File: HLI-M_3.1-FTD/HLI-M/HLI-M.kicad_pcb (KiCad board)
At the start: 2 copper layers, 124.2 x 84.7 mm, 119 parts, among them CON1 , CON2 USB_B, CON3 , CON4 Connector_Adapter, CON5 Connector_Audio, CON6 Conn_01x15, CON7 Conn_01x09, CON8 CR123A, Q1 IRLML5103, Q2 BC817, Q3 BC817, Q4 BSS84, Q5 BSS84, Q6 BSS84, Q7 BSS84, U1 PIC24HJ64GP206-I_PT, U10 24AA02-OT, U10-A SOIC-8_3.9x4.9mm_P1.27mm, U11 ULN2003, U12 ULN2003, U13 ULN2003, U2 SOIC-8_3.9x4.9mm_P1.27mm, U2-A DFN-8-1EP_6x5mm_P1.27mm_EP2x2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, U3 MAX3232, U4 TPS7A0533PDBV, U5 TPS7A0533PDBV, U6 VSON-10-1EP_3x3mm_P0.5mm_EP1.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, U8 FT232RL, U9 SOIC-8_3.9x4.9mm_P1.27mm, Y1 Crystal_32KHz, Y2 Crystal_20MHz

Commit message: att
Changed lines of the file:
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@@
     (fp_line (start -9.99 6.67) (end -9.99 -3.83) (layer "F.SilkS") (width 0.12))
     (fp_line (start -8.93 -4.89) (end 42.17 -4.89) (layer "F.SilkS") (width 0.12))
-    (fp_arc (start 33.851689 -2.79) (mid 35.123329 -2.197033) (end 35.48647 -0.841744) (layer "F.SilkS") (width 0.12))
+    (fp_arc (start 33.851689 -2.79) (mid 35.123331 -2.197031) (end 35.48647 -0.841744) (layer "F.SilkS") (width 0.12))
     (fp_arc (start 42.17 -4.89) (mid 42.919533 -4.579533) (end 43.23 -3.83) (layer "F.SilkS") (width 0.12))
     (fp_arc (start 43.23 6.67) (mid 42.919533 7.419533) (end 42.17 7.73) (layer "F.SilkS") (width 0.12))
-    (fp_arc (start 34.587202 4.258256) (mid 34.019453 5.24164) (end 32.952421 5.63) (layer "F.SilkS") (width 0.12))
+    (fp_arc (start 34.587202 4.258256) (mid 34.01945 5.241642) (end 32.952421 5.63) (layer "F.SilkS") (width 0.12))
     (fp_arc (start -8.93 7.73) (mid -9.679533 7.419533) (end -9.99 6.67) (layer "F.SilkS") (width 0.12))
     (fp_arc (start -2.24647 -0.841744) (mid -1.883323 -2.197028) (end -0.611689 -2.79) (layer "F.SilkS") (width 0.12))
@@
     (fp_arc (start 0.276073 5.57) (mid -0.752387 5.195671) (end -1.299619 4.247837) (layer "F.Fab") (width 0.1))
     (fp_arc (start 42.17 -4.83) (mid 42.877107 -4.537107) (end 43.17 -3.83) (layer "F.Fab") (width 0.1))
-    (fp_arc (start 33.863194 -2.73) (mid 35.088869 -2.158463) (end 35.438886 -0.852163) (layer "F.Fab") (width 0.1))
+    (fp_arc (start 33.863194 -2.73) (mid 35.08887 -2.158462) (end 35.438886 -0.852163) (layer "F.Fab") (width 0.1))
     (fp_arc (start -2.198886 -0.852163) (mid -1.848865 -2.15846) (end -0.623194 -2.73) (layer "F.Fab") (width 0.1))
     (fp_arc (start 43.17 6.67) (mid 42.877107 7.377107) (end 42.17 7.67) (layer "F.Fab") (width 0.1))
-    (fp_arc (start 34.539619 4.247837) (mid 33.99238 5.195662) (end 32.963927 5.57) (layer "F.Fab") (width 0.1))
+    (fp_arc (start 34.539619 4.247837) (mid 33.992389 5.195681) (end 32.963927 5.57) (layer "F.Fab") (width 0.1))
     (fp_arc (start -8.93 7.67) (mid -9.637107 7.377107) (end -9.93 6.67) (layer "F.Fab") (width 0.1))
     (fp_arc (start -9.93 -3.83) (mid -9.637107 -4.537107) (end -8.93 -4.83) (layer "F.Fab") (width 0.1))
@@
   (segment (start 187.6552 92.0242) (end 185.4746 89.8436) (width 1.5) (layer "B.Cu") (net 26))
   (segment (start 113.9571 109.1311) (end 116.1542 111.3282) (width 1.5) (layer "B.Cu") (net 26))
-  (segment (start 102.2604 110.998) (end 112.0902 110.998) (width 1.5) (layer "B.Cu") (net 26))
-  (segment (start 74.295 53.1368) (end 74.295 78.4352) (width 1.5) (layer "B.Cu") (net 26))
+  (segment (start 102.9716 110.998) (end 112.0902 110.998) (width 1.5) (layer "B.Cu") (net 26))
   (segment (start 162.4584 109.5248) (end 164.3634 111.4298) (width 1.5) (layer "B.Cu") (net 26))
-  (segment (start 112.0902 110.998) (end 113.9571 109.1311) (width 1.5) (layer "B.Cu") (net 26))
   (segment (start 164.3634 111.4298) (end 164.3634 111.4806) (width 1.5) (layer "B.Cu") (net 26))
   (segment (start 164.3634 111.4806) (end 173.7868 111.4806) (width 1.5) (layer "B.Cu") (net 26))
+  (segment (start 112.0902 110.998) (end 113.9571 109.1311) (width 1.5) (layer "B.Cu") (net 26))
   (segment (start 184.0992 67.4116) (end 181.7037 67.4116) (width 1.5) (layer "B.Cu") (net 26))
   (segment (start 185.4746 89.8436) (end 184.5564 89.8436) (width 1.5) (layer "B.Cu") (net 26))
   (segment (start 187.1218 70.4342) (end 184.0992 67.4116) (width 1.5) (layer "B.Cu") (net 26))
-  (segment (start 89.6874 93.8276) (end 89.6874 98.425) (width 1.5) (layer "B.Cu") (net 26))
   (segment (start 184.5564 89.8436) (end 184.7812 89.8436) (width 1.5) (layer "B.Cu") (net 26))
-  (segment (start 89.6874 98.425) (end 102.2604 110.998) (width 1.5) (layer "B.Cu") (net 26))
+  (segment (start 74.295 82.3214) (end 102.9716 110.998) (width 1.5) (layer "B.Cu") (net 26))
   (segment (start 92.4589 38.862) (end 79.0448 38.862) (width 1.5) (layer "B.Cu") (net 26))
   (segment (start 96.5454 34.7755) (end 92.4589 38.862) (width 1.5) (layer "B.Cu") (net 26))
   (segment (start 74.295 43.6118) (end 74.295 53.1368) (width 1.5) (layer "B.Cu") (net 26))
-  (segment (start 74.295 78.4352) (end 89.6874 93.8276) (width 1.5) (layer "B.Cu") (net 26))
   (segment (start 187.1218 87.503) (end 187.1218 70.4342) (width 1.5) (layer "B.Cu") (net 26))
+  (segment (start 74.295 53.1368) (end 74.295 82.3214) (width 1.5) (layer "B.Cu") (net 26))
   (segment (start 160.655 111.3282) (end 162.4584 109.5248) (width 1.5) (layer "B.Cu") (net 26))
   (segment (start 187.6552 97.6122) (end 187.6552 92.0242) (width 1.5) (layer "B.Cu") (net 26))

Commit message: atualizado hli-m, precisa de revisao
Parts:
- added RT3: 0.5A, Resistor_SMD:R_1812_4532Metric, F.Cu at (74.3, 44.5)
- L1: renamed from L2; value BLM21PG221SN1D -> BBPY0020
- Q1: value IRLML5103 -> DMP3068L-7
- R4: value 10k -> 22k
- moved RT1 8.34 mm to (98.3, 44.4)
- moved LED1 7.00 mm to (88.6, 45.5), turned to 180 degrees
- moved R5 4.03 mm to (167.6, 70.7), turned to 0 degrees
- moved C14 3.97 mm to (167.6, 66.6), turned to 180 degrees
- moved C1 2.99 mm to (98.0, 52.4)
- moved C2 2.99 mm to (100.2, 52.4)
- moved C3 2.99 mm to (102.3, 52.3)
- moved R1 2.84 mm to (84.8, 45.5)
- moved R21 2.60 mm to (133.3, 91.6)
- moved C4 1.17 mm to (117.2, 50.4)
- moved L1 1.17 mm to (119.2, 50.5)
- moved R22 1.09 mm to (131.5, 91.6)
- moved Q5 0.86 mm to (132.6, 95.8), turned to -90 degrees
- moved C13 0.33 mm to (167.6, 68.6), turned to 0 degrees
- moved CON1 0.30 mm to (88.6, 34.8)
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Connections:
- C21 pad 1: Net-(U1-Pad40) -> Net-(C21-Pad1)
- C22 pad 1: Net-(U1-Pad39) -> Net-(C22-Pad1)
- CON1 pad 1: +5V -> Net-(CON1-Pad1)
- CON3 pad 23: K_E -> 0
- CON8 pad N: (no net) -> 0
- U1 pad 4: Net-(C18-Pad1) -> Net-(C14-Pad1)
- U1 pad 56: Net-(C24-Pad1) (its old number) -> Net-(C19-Pad1)
- U2 pad 3: Net-(R16-Pad2) -> Net-(R5-Pad2)
- U2 pad 6: Net-(C18-Pad1) -> Net-(C14-Pad1)
- U2 pad 7: Net-(R16-Pad2) -> Net-(R5-Pad2)
- U2-A pad 3: Net-(R16-Pad2) -> Net-(R5-Pad2)
- U2-A pad 6: Net-(C18-Pad1) -> Net-(C14-Pad1)
- U2-A pad 7: Net-(R16-Pad2) -> Net-(R5-Pad2)
- U6 pad 8: Net-(R4-Pad2) -> Net-(R2-Pad2)
- U6 pad 9: Net-(R5-Pad1) -> Net-(R3-Pad1)
- Y2 pad 1: Net-(U1-Pad39) -> Net-(C22-Pad1)
- Y2 pad 3: Net-(U1-Pad40) -> Net-(C21-Pad1)
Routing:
- net +12V: track 261.5 -> 352.8 mm, vias 1 -> 5
- net Net-(C14-Pad1): track 0.00 -> 30.3 mm, vias 0 -> 2
- net Net-(R5-Pad2): track 0.00 -> 26.6 mm, vias 0 -> 2
- net Net-(C18-Pad1): track 23.5 -> 0.00 mm, vias 2 -> 0
- net K_E: track 24.6 -> 1.38 mm
- net Net-(R16-Pad2): track 16.8 -> 0.00 mm
- net +5V: track 243.3 -> 259.2 mm, vias 0 -> 2
- net Net-(CON1-Pad1): track 0.00 -> 12.5 mm
- net Net-(U1-Pad39): track 10.4 -> 0.00 mm
- net Net-(C22-Pad1): track 0.00 -> 10.4 mm
- net Net-(CON3-Pad24): track 52.5 -> 44.2 mm
- net Net-(U1-Pad40): track 7.80 -> 0.00 mm
- net Net-(C21-Pad1): track 0.00 -> 7.80 mm
- net +3V3: track 293.1 -> 286.7 mm, vias 28 -> 29
- net Net-(R2-Pad2): track 0.00 -> 4.99 mm
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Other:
- board size 124.2 x 84.7 mm -> 125.2 x 85.6 mm

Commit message: att
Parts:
- removed G***: LOGO, LOGO
- removed RT3: 0.5A, Resistor_SMD:R_1812_4532Metric
- added F1: Fuse, Fuse:Fuse_1812_4532Metric, F.Cu at (71.3, 44.9)
- added RV1: Varistor, Capacitor_SMD:C_0603_1608Metric_Pad1.08x0.95mm_HandSolder, F.Cu at (76.0, 45.9)
- CON5: value Connector_Audio -> Connector_note; footprint Connector_JST:JST_EH_B3B-EH-A_1x03_P2.50mm_Vertical -> Connector_IDC:IDC-Header_2x04_P2.54mm_Horizontal
- moved G1 104.6 mm to (93.3, 108.3)
- moved CON5 18.9 mm to (180.4, 76.5), turned to 0 degrees
- moved CON4 14.3 mm to (180.6, 48.1)
- moved LED1 2.06 mm to (90.6, 44.9)
- moved R1 2.06 mm to (86.8, 44.9)
- moved R8 1.62 mm to (175.6, 87.8)
- moved R9 1.62 mm to (177.4, 87.8)
- moved CON8 0.97 mm to (83.5, 80.7)
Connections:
- CON5 pad 2: 0 -> INIB
- CON5 pad 3: +12V -> RXA
- CON8 pad P: (no net) -> Net-(CON8-Pad1)
- U1 pad 17: Net-(R9-Pad1) -> Net-(R7-Pad1)
- U1 pad 44: (no net) -> EXTERN_D10
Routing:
- net PRINT_IMP: track 15.7 -> 114.0 mm
- net INIB: track 27.3 -> 124.6 mm, vias 1 -> 2
- net NOTE_: track 14.8 -> 80.8 mm, vias 0 -> 2
- net RXA: track 43.5 -> 106.0 mm, vias 2 -> 3
- net EXTERN_D10: track 0.00 -> 59.4 mm, vias 0 -> 2
- net TXA: track 46.0 -> 96.1 mm, vias 2 -> 5
- net Net-(R7-Pad1): track 0.00 -> 35.2 mm, vias 0 -> 2
- net Net-(R9-Pad1): track 33.7 -> 0.00 mm, vias 2 -> 0
- net +5V: track 259.2 -> 235.9 mm
- net PGED2: track 45.0 -> 66.7 mm
- net PGEC2: track 43.7 -> 64.7 mm
- net VBAT: track 208.2 -> 223.8 mm
- net RESET: track 33.8 -> 44.7 mm
- net +3V3: track 286.7 -> 295.7 mm
- net TXP: track 85.1 -> 76.3 mm
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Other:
- board size 125.2 x 85.6 mm -> 125.2 x 86.4 mm

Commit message: att projeto
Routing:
- net +12V: track 360.9 -> 393.0 mm, vias 5 -> 6
- net EXTERN_D10: track 59.4 -> 57.5 mm
- net 0: vias 45 -> 46

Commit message: atualização circuito FTD e 3D
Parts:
- added R29: 470R, Resistor_SMD:R_0603_1608Metric_Pad0.98x0.95mm_HandSolder, F.Cu at (107.3, 58.8)
- added R30: 470R, Resistor_SMD:R_0603_1608Metric_Pad0.98x0.95mm_HandSolder, F.Cu at (104.8, 58.8)
- C21, C22: value 10pF -> 20pF
- C23, C24: value 7pF -> 12pF
- moved RV1 6.94 mm to (71.3, 51.0), turned to 0 degrees
- moved LED1 1.82 mm to (90.8, 46.7)
- moved R1 1.82 mm to (87.0, 46.7)
- moved F1 1.55 mm to (71.5, 46.4)
- moved C10 1.27 mm to (100.7, 68.8)
- moved R17 1.18 mm to (140.0, 57.4)
- moved C2 1.09 mm to (99.1, 52.3)
- moved U8 1.09 mm to (109.0, 51.3)
- moved C3 1.09 mm to (101.2, 52.3)
- moved C1 1.09 mm to (96.9, 52.3)
- moved Q3 0.94 mm to (140.1, 60.5)
- moved R18 0.73 mm to (140.2, 63.7)
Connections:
- C14 pad 1: Net-(C14-Pad1) -> Net-(U1-SCK2/RG6)
- C19 pad 1: Net-(C19-Pad1) -> Net-(U1-VDDCORE)
- C20 pad 1: Net-(C19-Pad1) -> Net-(U1-VDDCORE)
- C23 pad 1: Net-(C23-Pad1) -> Net-(U1-RC14)
- C24 pad 1: Net-(C24-Pad1) -> Net-(U1-RC13)
- C8 pad 1: Net-(C8-Pad1) -> Net-(U6-USB_SEL)
- CON8 pad P: Net-(CON8-Pad1) -> (no net)
- R12 pad 2: Net-(C19-Pad1) -> Net-(U1-VDDCORE)
- R2 pad 2: Net-(R2-Pad2) -> Net-(U6-ISET)
- R3 pad 1: Net-(R3-Pad1) -> Net-(U6-TS)
- R5 pad 2: Net-(R5-Pad2) -> Net-(U2-*HOLD)
- R6 pad 1: Net-(R6-Pad1) -> Net-(U1-RD8)
- R7 pad 1: Net-(R7-Pad1) -> Net-(U1-RB6)
- RT2 pad 1: Net-(CON8-Pad1) -> Net-(CON8-+)
- U3 pad 11: Net-(U1-Pad33) -> Net-(U1-U1TX/RF3)
- U3 pad 12: Net-(U1-Pad34) -> Net-(U1-U1RX/RF2)
- U8 pad 1: TXA -> Net-(U8-TXD)
- U8 pad 5: RXA -> Net-(U8-RXD)
- Y1 pad 1: Net-(C23-Pad1) -> Net-(U1-RC14)
- Y1 pad 2: Net-(C24-Pad1) -> Net-(U1-RC13)
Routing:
- net Net-(CON8-Pad1): track 19.2 -> 0.00 mm
- net Net-(CON8-+): track 0.00 -> 19.2 mm
- net Net-(U1-Pad39): track 0.00 -> 10.4 mm
- net Net-(U1-OSC1/CLKIN): track 10.4 -> 0.00 mm
- net Net-(U1-Pad40): track 0.00 -> 7.80 mm
- net Net-(U1-OSC2/CLKO): track 7.80 -> 0.00 mm
- net +5V: track 235.9 -> 240.5 mm
- net +5VL: track 56.6 -> 60.4 mm
- net Net-(U8-TXD): track 0.00 -> 3.34 mm
- net Net-(U8-RXD): track 0.00 -> 3.03 mm
- net Net-(CON1-Pin_1): track 15.2 -> 18.0 mm
- net RXA: track 106.0 -> 104.1 mm
- net +3V3: track 295.7 -> 294.0 mm
- net TXA: track 96.1 -> 94.7 mm
- net INIB: track 124.6 -> 123.4 mm
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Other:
- board size 125.2 x 86.4 mm -> 125.2 x 86.1 mm
- board text added: "Made in China"
- board text removed: "Designed in Brazil. Made in China"

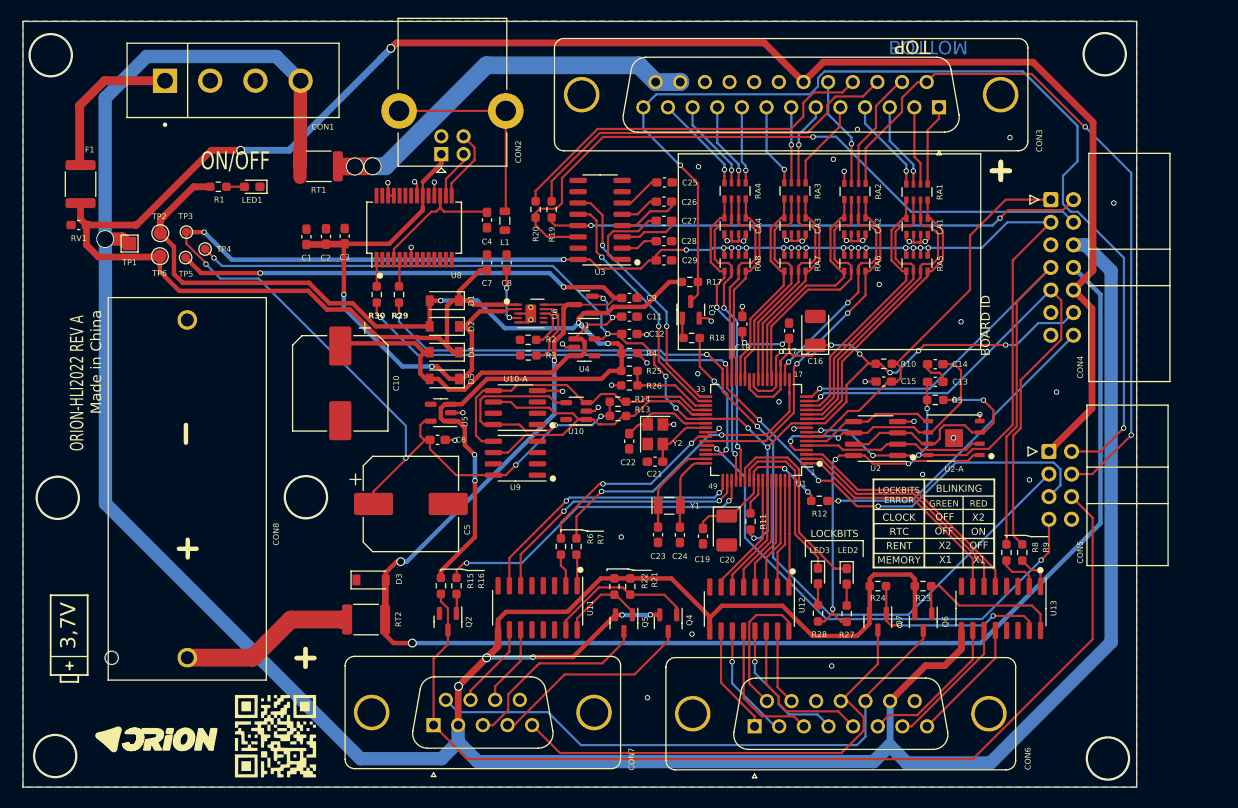
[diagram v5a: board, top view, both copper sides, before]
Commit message: HLI-M_2023: circuito atualizado e revisado.
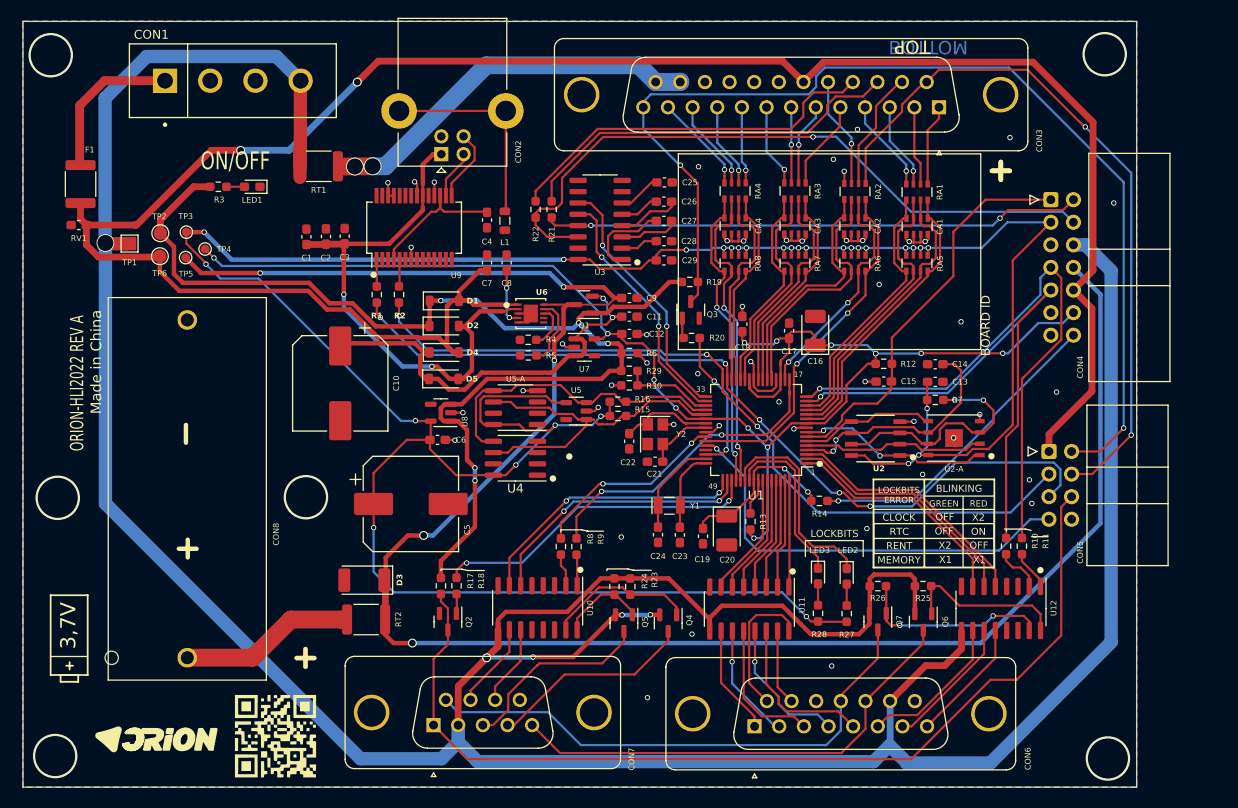
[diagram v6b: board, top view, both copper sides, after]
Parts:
- CON1: footprint 6:Molex-0015244449-0 -> Footprint_HLI-M:Molex-0015244449-0
- CON4: value Connector_Adapter -> Con_ADAPTER
- CON5: value Connector_note -> Con_MULTLINKER
- D3: footprint Diode_SMD:D_SOD-123 -> Diode_SMD:D_2010_5025Metric
- Q4, Q5, Q6, Q7: value BSS84 -> DMP2305
- R4: renamed from R2; value 10k -> 3,3K
- U1: value PIC24HJ64GP206-I_PT -> PIC24HJ64GP206
- U2: value SOIC-8_3.9x4.9mm_P1.27mm -> FM25V10; footprint Package_SO:SOIC-8_3.9x4.9mm_P1.27mm -> Footprint_HLI-M:FM25V10-GTR
- U4: renamed from U9; value SOIC-8_3.9x4.9mm_P1.27mm -> ATSHA204A-SSHDA-B
- U6: value VSON-10-1EP_3x3mm_P0.5mm_EP1.2x2mm_ThermalVias -> LM3658SD; footprint Package_SON:VSON-10-1EP_3x3mm_P0.5mm_EP1.2x2mm_ThermalVias -> Footprint_HLI-M:LM3658SD
- moved D3 0.76 mm to (103.4, 90.9), turned to 180 degrees
- moved R10 0.71 mm to (175.6, 87.1)
- moved R11 0.71 mm to (177.3, 87.1)
- moved D5 0.08 mm to (112.3, 68.3), turned to 0 degrees
- moved D2 0.06 mm to (112.4, 62.4), turned to 0 degrees
- turned D4 to 0 degrees
- turned D1 to 0 degrees
- renumbered C24 to C23, C23 to C24, R30 to R1, R8 to R10, R9 to R11, R10 to R12, R11 to R13, R12 to R14, R13 to R15, R14 to R16, R15 to R17, R16 to R18, R17 to R19, R29 to R2, R18 to R20, R19 to R21, R20 to R22, R21 to R23, R22 to R24, R23 to R25, R24 to R26, R25 to R29, R1 to R3, R26 to R30, R3 to R5, R4 to R6, R5 to R7, R6 to R8, R7 to R9, U11 to U10, U12 to U11, U13 to U12, U10 to U5, U10-A to U5-A, U4 to U7, U5 to U8, U8 to U9
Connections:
- C10 pad 1: Net-(D4-A) -> Net-(D4-K)
- C11 pad 1: Net-(D4-A) -> Net-(D4-K)
- C23 pad 1: Net-(U1-RC13) -> Net-(U1-RC14)
- C24 pad 1: Net-(U1-RC14) -> Net-(U1-RC13)
- CON6 pad 12: COUT -> CIN
- CON6 pad 13: CIN -> COUT
- CON8 pad P: (no net) -> Net-(CON8-+)
- D1 pad 1: +5V -> +5VD
- D1 pad 2: +5VD -> +5V
- D2 pad 1: +5VL -> +5VD
- D2 pad 2: +5VD -> +5VL
- D3 pad 1: 0 -> VBAT
- D3 pad 2: VBAT -> 0
- D4 pad 1: +5V -> Net-(D4-K)
- D4 pad 2: Net-(D4-A) -> +5V
- D5 pad 1: +5VL -> Net-(D4-K)
- D5 pad 2: Net-(D4-A) -> +5VL
- Q1 pad 2: Net-(D4-A) -> Net-(D4-K)
- Q6 pad 3: CIN -> COUT
- Q7 pad 3: COUT -> CIN
- R10 pad 1: PGED2 -> PGEC2
- R10 pad 2: PIN-CIN -> PIN-COUT
- R11 pad 1: PGEC2 -> PGED2
- R11 pad 2: PIN-COUT -> PIN-CIN
- R13 pad 2: Net-(R11-Pad2) -> Net-(R13-Pad2)
- U1 pad 17: Net-(R7-Pad1) -> Net-(U1-RB6)
- U1 pad 33: Net-(U1-Pad33) -> Net-(U1-U1TX/RF3)
- U1 pad 34: Net-(U1-Pad34) -> Net-(U1-U1RX/RF2)
- U1 pad 39: Net-(U1-Pad39) -> Net-(U1-OSC1/CLKIN)
- U1 pad 4: Net-(C14-Pad1) -> Net-(U1-SCK2/RG6)
- U1 pad 40: Net-(U1-Pad40) -> Net-(U1-OSC2/CLKO)
- U1 pad 42: Net-(R6-Pad1) -> Net-(U1-RD8)
- U1 pad 47: Net-(C23-Pad1) -> Net-(U1-RC13)
- U1 pad 48: Net-(C24-Pad1) -> Net-(U1-RC14)
- U1 pad 56: Net-(C19-Pad1) -> Net-(U1-VDDCORE)
- U1 pad 57: Net-(R15-Pad2) -> Net-(R13-Pad2)
- U12 pad 1: PIN-COUT -> PIN-CIN
- U12 pad 2: PIN-CIN -> PIN-COUT
- U2 pad 3: Net-(R5-Pad2) -> Net-(U2-*HOLD)
- U2 pad 6: Net-(C14-Pad1) -> Net-(U1-SCK2/RG6)
- U2 pad 7: Net-(R5-Pad2) -> Net-(U2-*HOLD)
- U2-A pad 3: Net-(R5-Pad2) -> Net-(U2-*HOLD)
- U2-A pad 6: Net-(C14-Pad1) -> Net-(U1-SCK2/RG6)
- U2-A pad 7: Net-(R5-Pad2) -> Net-(U2-*HOLD)
- U6 pad 4: Net-(C8-Pad1) -> Net-(U6-USB_SEL)
- U6 pad 8: Net-(R2-Pad2) -> Net-(U6-ISET)
- U6 pad 9: Net-(R3-Pad1) -> Net-(U6-TS)
- U7 pad 1: Net-(D4-A) -> Net-(D4-K)
- U7 pad 3: Net-(D4-A) -> Net-(D4-K)
- Y1 pad 1: Net-(U1-RC14) -> Net-(U1-RC13)
- Y1 pad 2: Net-(U1-RC13) -> Net-(U1-RC14)
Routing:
- net Net-(D4-K): track 0.00 -> 48.1 mm, vias 0 -> 2
- net Net-(D4-A): track 48.1 -> 0.00 mm, vias 2 -> 0
- net +3V3: track 294.0 -> 331.8 mm
- net Net-(U1-RB6): track 0.00 -> 35.2 mm, vias 0 -> 2
- net Net-(R7-Pad1): track 35.2 -> 0.00 mm, vias 2 -> 0
- net Net-(C14-Pad1): track 30.7 -> 0.00 mm, vias 2 -> 0
- net Net-(U1-U1TX/RF3): track 0.00 -> 28.9 mm, vias 0 -> 2
- net Net-(U1-Pad33): track 28.9 -> 0.00 mm, vias 2 -> 0
- net Net-(U1-U1RX/RF2): track 0.00 -> 28.2 mm, vias 0 -> 2
- net Net-(U1-Pad34): track 28.2 -> 0.00 mm, vias 2 -> 0
- net Net-(U1-SCK2/RG6): track 0.00 -> 27.2 mm, vias 0 -> 2
- net Net-(U2-*HOLD): track 0.00 -> 26.8 mm, vias 0 -> 2
- net Net-(R5-Pad2): track 26.6 -> 0.00 mm, vias 2 -> 0
- net Net-(U1-RD8): track 0.00 -> 22.1 mm, vias 0 -> 2
- net Net-(R6-Pad1): track 22.1 -> 0.00 mm, vias 2 -> 0
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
